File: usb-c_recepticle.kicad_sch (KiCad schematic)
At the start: 4 parts, among them J2 USB_C_Receptacle_USB2.0_16P, U7 USBLC6-2SC6

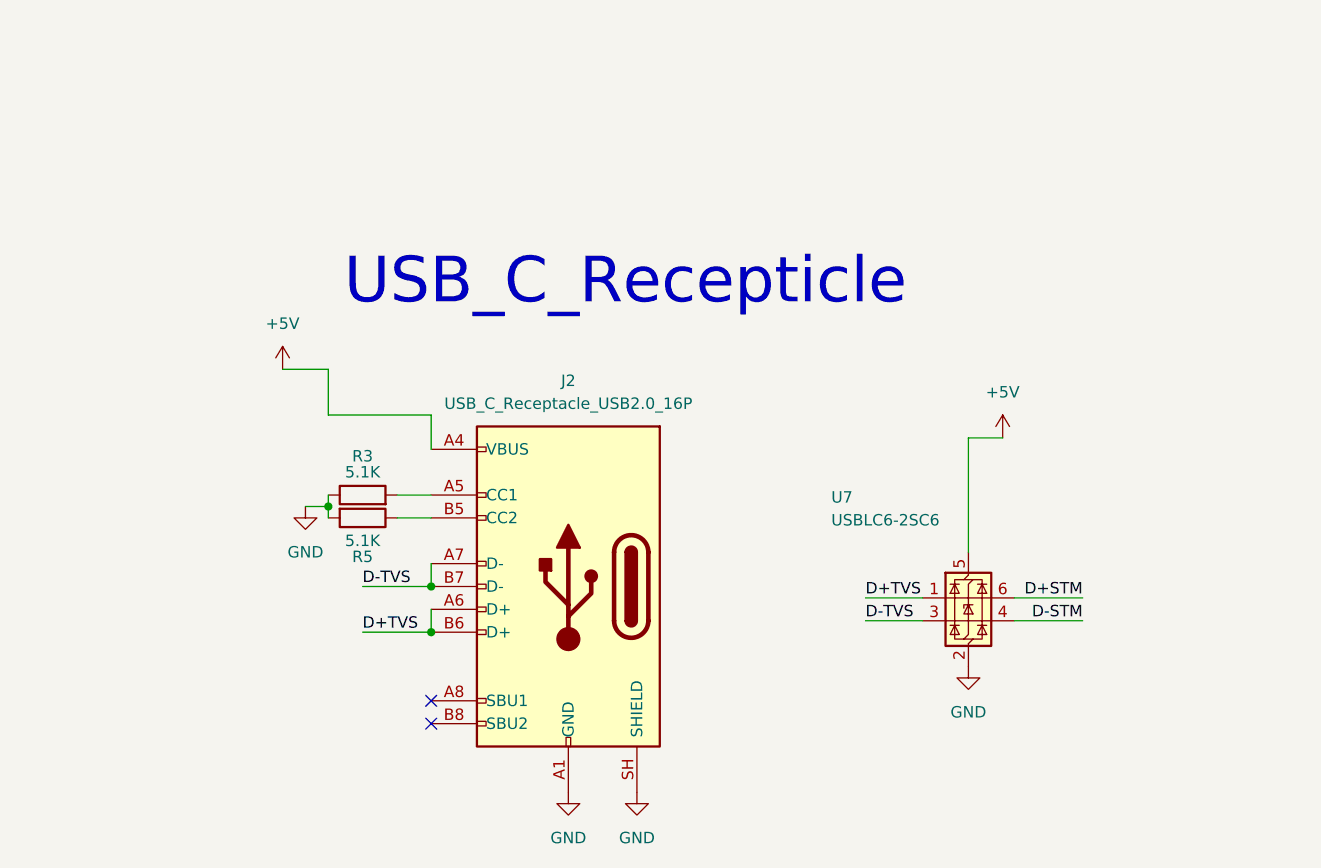
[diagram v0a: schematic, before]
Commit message: Fixed GPS, Radio, Baro, STM32, and added/rearanged some sheets (#26)
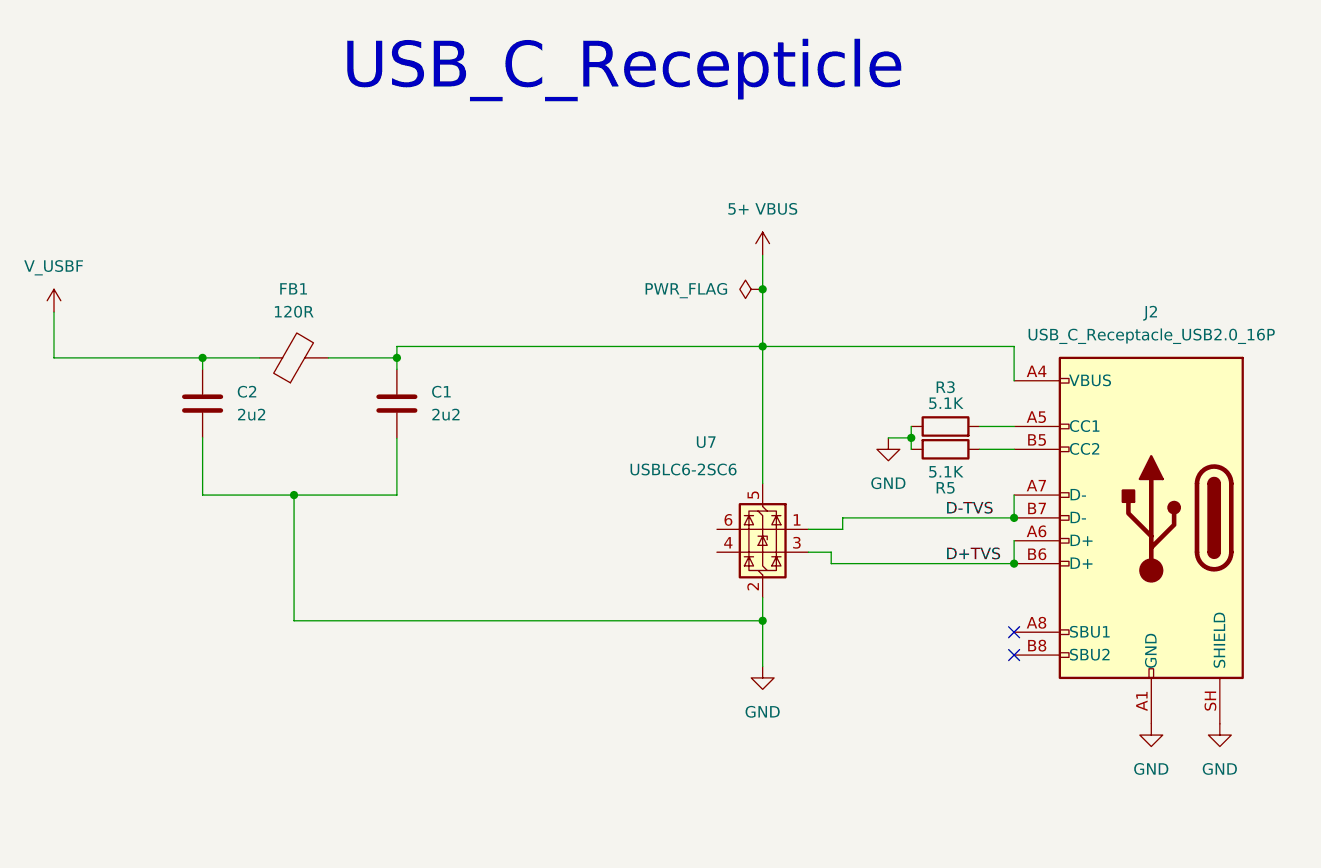
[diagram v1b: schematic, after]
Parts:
- added C1, C2: 2u2, symbol Device:C
- added FB1: 120R, symbol Device:FerriteBead
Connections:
- net D+TVS: now also U7.3 (I/O2); no longer U7.1 (I/O1)
- net D-TVS: now also U7.1 (I/O1); no longer U7.3 (I/O2)
- net GND: now also C1.2, C2.2
- net +5V renamed 5+ VBUS
- net 5+ VBUS: now also C1.1, FB1.2
- net D+STM: no longer names the net of U7.6 (I/O1)
- net D-STM: no longer names the net of U7.4 (I/O2)
- new net V_USBF: C2.1, FB1.1
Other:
- moved on the sheet: J2, R3, R5
